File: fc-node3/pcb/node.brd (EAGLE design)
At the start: 48 x 23 mm, 22 parts, among them IC1 HTU21D, J1 AVR_SPI_PRG_62X3_LOCK, U1 ATTINY84, U2 MCP1640, U3 BU49X_VDET_SOT235, U5 DS18B20

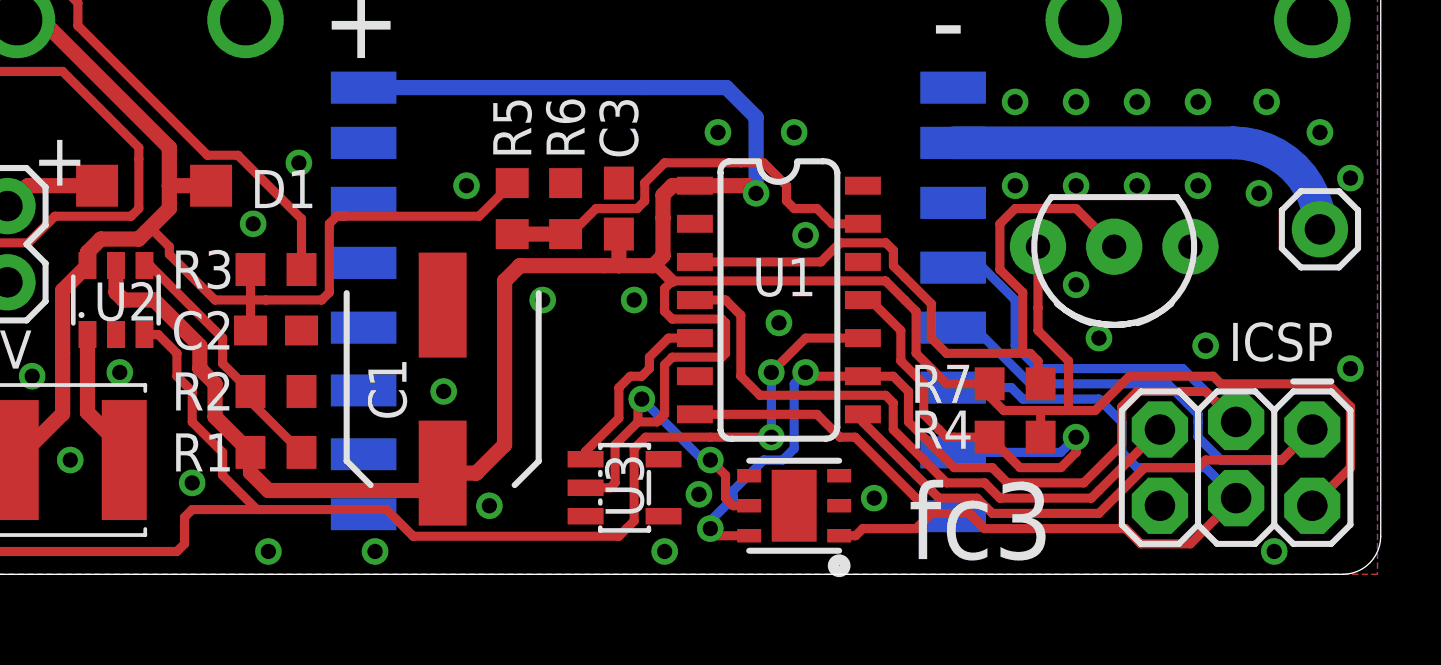
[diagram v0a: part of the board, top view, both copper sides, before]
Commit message: power ds18b20 from avr pin
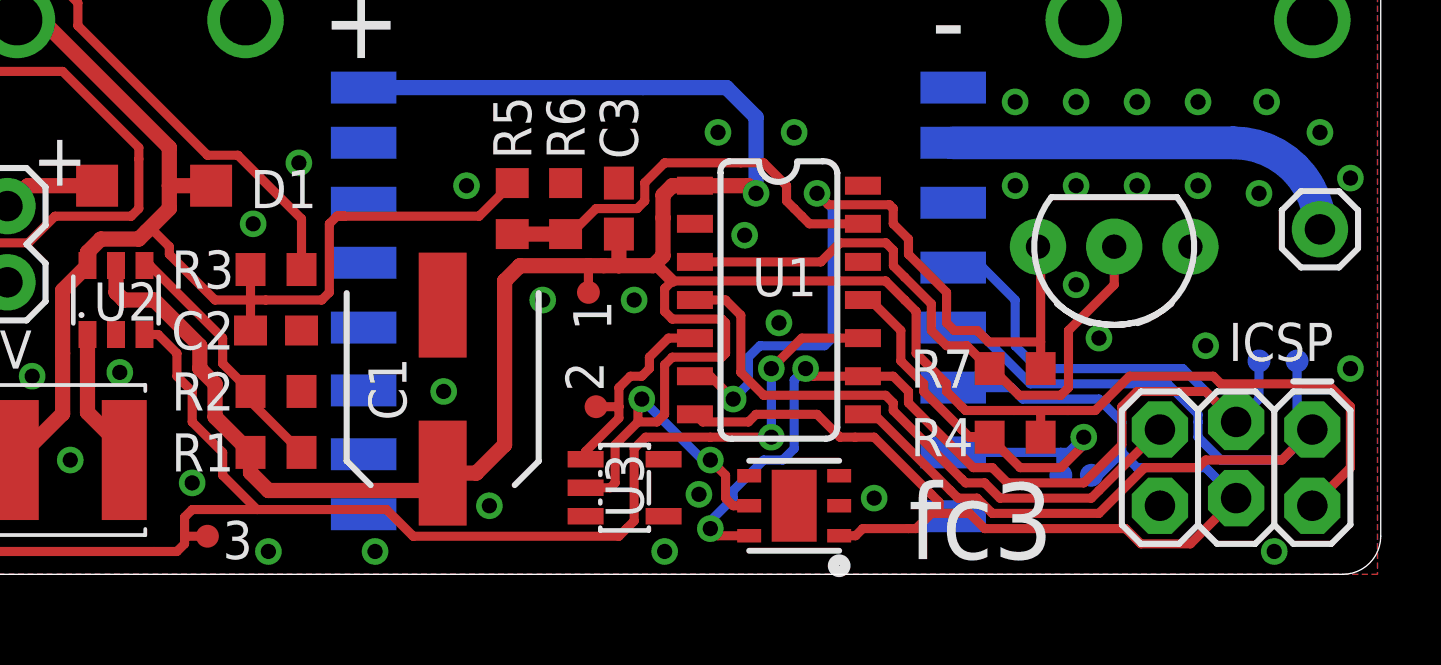
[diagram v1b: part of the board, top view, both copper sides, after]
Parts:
- added TP1, TP2, TP3, TP4, TP5, TP6, TP7: TEST-POINT3, SparkFun-Passives:PAD.03X.03
- moved R7 0.51 mm to (35.8, 6.86), turned to 0 degrees
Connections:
- removed net N$6: U1.6
- new net 18B20_VDD: R7.2, U1.6, U5.3
- net DET: now also TP2.P$1
- net EN: now also TP3.P$1
- net MISO: now also TP6.P$1
- net MOSI: now also TP5.P$1
- net RFM_SS: now also TP4.P$1
- net SCK: now also TP7.P$1
- net VCC: now also TP1.P$1; no longer R7.2, U5.3
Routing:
- net 18B20_VDD: track 0.00 -> 26.1 mm, vias 0 -> 2
- net VCC: track 109.1 -> 104.0 mm
- net 18B20_DQ: track 24.3 -> 21.1 mm
- net MISO: track 32.3 -> 34.7 mm
- net SCK: track 39.6 -> 41.8 mm
- net MOSI: track 35.8 -> 37.8 mm
- net RFM_SS: track 15.6 -> 16.8 mm
- net EN: track 89.0 -> 89.9 mm
- net DET: track 6.29 -> 7.05 mm
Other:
- board text added: "1"
- board text added: "2"
- board text added: "3"
- board text added: "4"
- board text added: "5"
- board text added: "6"
- board text added: "7"
- board text added: "Ensure Isc <= (battery capacity)/10"
- board text added: "SOLAR PANEL"

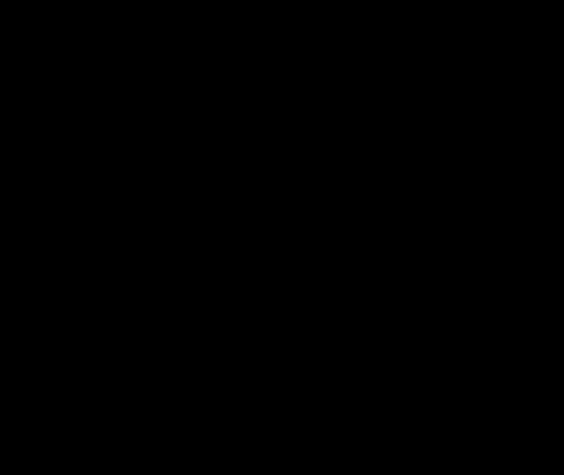
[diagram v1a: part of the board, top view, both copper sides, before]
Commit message: pullups i2c on fc3
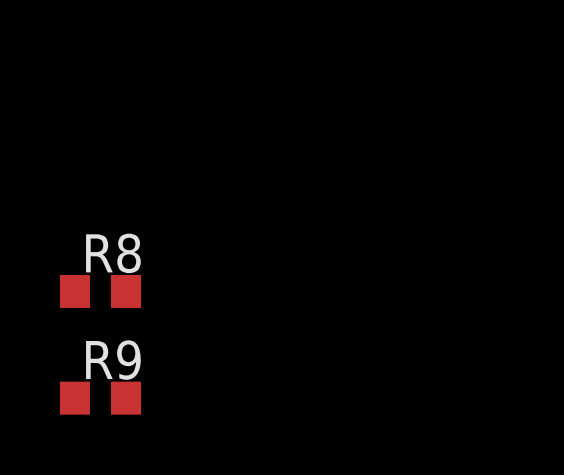
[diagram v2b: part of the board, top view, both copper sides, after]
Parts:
- added R8, R9: (no value), rcl:R0603
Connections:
- net MOSI: now also R9.1
- net SCK: now also R8.1
- net VCC: now also R8.2, R9.2
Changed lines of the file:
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@@
 <element name="TP6" library="SparkFun-Passives" package="PAD.03X.03" value="TEST-POINT3" x="45.212" y="7.112" rot="MR0"/>
 <element name="TP7" library="SparkFun-Passives" package="PAD.03X.03" value="TEST-POINT3" x="43.942" y="7.112" rot="MR0"/>
+<element name="R8" library="rcl" package="R0603" value="" x="0.254" y="-17.526"/>
+<element name="R9" library="rcl" package="R0603" value="" x="0.254" y="-21.082"/>
 </elements>
 <signals>
@@
 <wire x1="36.664" y1="4.572" x2="36.664" y2="5.373" width="0.3048" layer="1"/>
 <wire x1="36.664" y1="5.373" x2="36.576" y2="5.461" width="0.3048" layer="1"/>
+<contactref element="R8" pad="2"/>
+<contactref element="R9" pad="2"/>
+<wire x1="1.104" y1="-17.526" x2="1.104" y2="-21.082" width="0" layer="19" extent="1-1"/>
+<wire x1="10.922" y1="2.794" x2="1.104" y2="-17.526" width="0" layer="19" extent="1-1"/>
 </signal>
 <signal name="N$1">
@@
 <wire x1="33.02" y1="2.667" x2="33.274" y2="2.413" width="0.3048" layer="1"/>
 <wire x1="33.274" y1="2.413" x2="33.274" y2="2.032" width="0.3048" layer="1"/>
+<contactref element="R9" pad="1"/>
+<wire x1="-0.596" y1="-21.082" x2="25.4" y2="5.08" width="0" layer="19" extent="1-1"/>
 </signal>
 <signal name="EN">
@@
 <wire x1="43.942" y1="7.112" x2="43.942" y2="5.842" width="0.3048" layer="16"/>
 <wire x1="43.942" y1="5.842" x2="43.18" y2="5.08" width="0.3048" layer="16"/>
+<contactref element="R8" pad="1"/>
+<wire x1="-0.596" y1="-17.526" x2="25.654" y2="1.524" width="0" layer="19" extent="1-1"/>
 </signal>
 <signal name="N$5">

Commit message: layout for fc3 r1.1
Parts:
- removed R8, R9: (no value), rcl:R0603
- moved R5 17.6 mm to (35.8, 6.86), turned to 0 degrees
- moved R7 16.1 mm to (20.6, 12.2), turned to 270 degrees
- moved C3 4.02 mm to (21.3, 8.38), turned to 270 degrees
- moved TP1 3.07 mm to (19.2, 11.3)
- moved R6 1.52 mm to (22.4, 12.2)
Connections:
- removed net VSENSE: R5.1, R6.2, U1.13
- net 18B20_DQ: now also R5.1; no longer R7.1
- net 18B20_VDD: now also R5.2; no longer R7.2
- net GND: no longer R6.1
- net MOSI: now also R7.1; no longer R9.1
- net SCK: now also R6.1; no longer R8.1
- net VBATT: now also U1.13; no longer R5.2
- net VCC: now also R6.2, R7.2; no longer R8.2, R9.2
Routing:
- net MOSI: track 37.8 -> 60.0 mm, vias 0 -> 1
- net SCK: track 41.8 -> 57.5 mm, vias 2 -> 3
- net VSENSE: track 14.2 -> 0.00 mm
- net VBATT: track 40.4 -> 53.6 mm
- net VCC: track 104.0 -> 106.1 mm
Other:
- board text added: "APRIL 2017"
- board text added: "r1.1"
- board text removed: "SEPTEMBER 2016"
